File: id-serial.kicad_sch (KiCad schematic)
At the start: 5 parts, among them IC17 AT24CS01_SOT23

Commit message: [#83358] Update KiCad project files
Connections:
- net 3V3_SYS: now also D15.1 (C); no longer D15.A
- net EEPROM_PWR: no longer D15.K

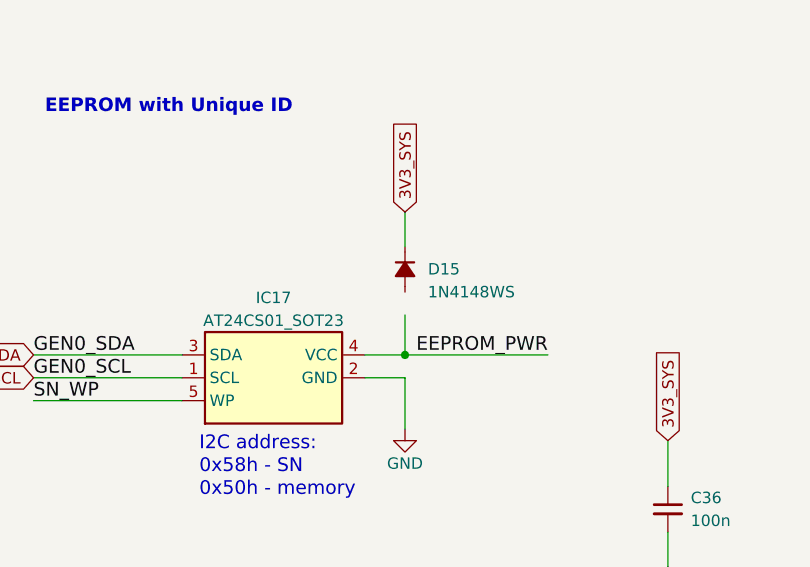
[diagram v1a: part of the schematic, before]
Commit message: [#83358] Repair broken symbol after update
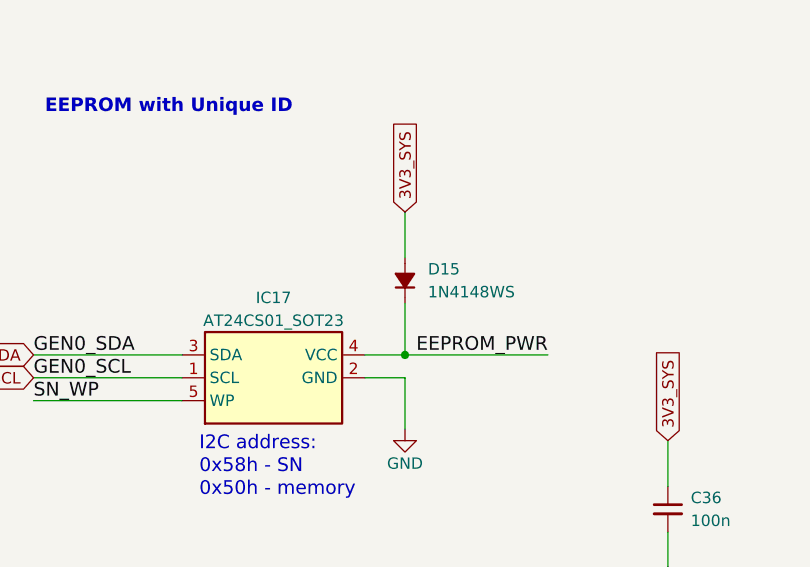
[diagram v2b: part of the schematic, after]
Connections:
- net 3V3_SYS: now also D15.2 (A); no longer D15.1 (C)
- net EEPROM_PWR: now also D15.1 (C)
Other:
- moved on the sheet: D15
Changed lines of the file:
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@@
 	(wire
 		(pts
-			(xy 218.44 104.14) (xy 218.44 107.95)
+			(xy 218.44 104.14) (xy 218.44 109.22)
 		)
 		(stroke
@@
 	(wire
 		(pts
-			(xy 218.44 115.57) (xy 218.44 120.015)
+			(xy 218.44 114.3) (xy 218.44 120.015)
 		)
 		(stroke
@@
 	(symbol
 		(lib_id "antmicroDiodesRectifiersSingle:1N4148WS")
-		(at 218.44 107.95 270)
+		(at 218.44 114.3 90)
 		(unit 1)
 		(exclude_from_sim no)
@@
 					(size 1.27 1.27)
 				)
-				(justify left)
+				(justify right)
 			)
 		)
 		(property "Value" "1N4148WS"
-			(at 219.7862 105.918 0)
+			(at 217.0938 116.332 0)
 			(effects
 				(font
@@
 		)
 		(property "Footprint" "antmicro-footprints:D_SOD-323F"
-			(at 218.44 107.95 0)
+			(at 218.44 114.3 0)
 			(effects
 				(font
@@
 		)
 		(property "Datasheet" "https://www.onsemi.com/pub/Collateral/1N914BWS-D.pdf"
-			(at 218.44 107.95 0)
+			(at 218.44 114.3 0)
 			(effects
 				(font
@@
 		)
 		(property "Description" ""
-			(at 218.44 107.95 0)
+			(at 218.44 114.3 0)
 			(effects
 				(font
@@
 		)
 		(property "Manufacturer" "ON Semiconductor"
-			(at 218.44 107.95 0)
+			(at 218.44 114.3 0)
 			(effects
 				(font
@@
 					(size 1.27 1.27)
 				)
-				(justify left)
+				(justify right)
 			)
 		)
 		(property "Author" "Antmicro"
-			(at 198.12 129.54 0)
+			(at 238.76 92.71 0)
 			(effects
 				(font
@@
 		)
 		(property "License" "Apache-2.0"
-			(at 195.58 129.54 0)
+			(at 241.3 92.71 0)
 			(effects
 				(font

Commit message: [#83366] Remove SoM and Tag Connect from vis
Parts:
- TP30: now left out of the parts list
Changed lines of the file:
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@@
 		(unit 1)
 		(exclude_from_sim no)
-		(in_bom yes)
+		(in_bom no)
 		(on_board yes)
 		(dnp no)
